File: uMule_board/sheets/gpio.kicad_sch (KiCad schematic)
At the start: 5 parts, among them J10 Conn_02x04_Odd_Even, J11 Conn_01x04, J12 Conn_01x04, J13 Conn_01x04, J9 Conn_02x04_Odd_Even

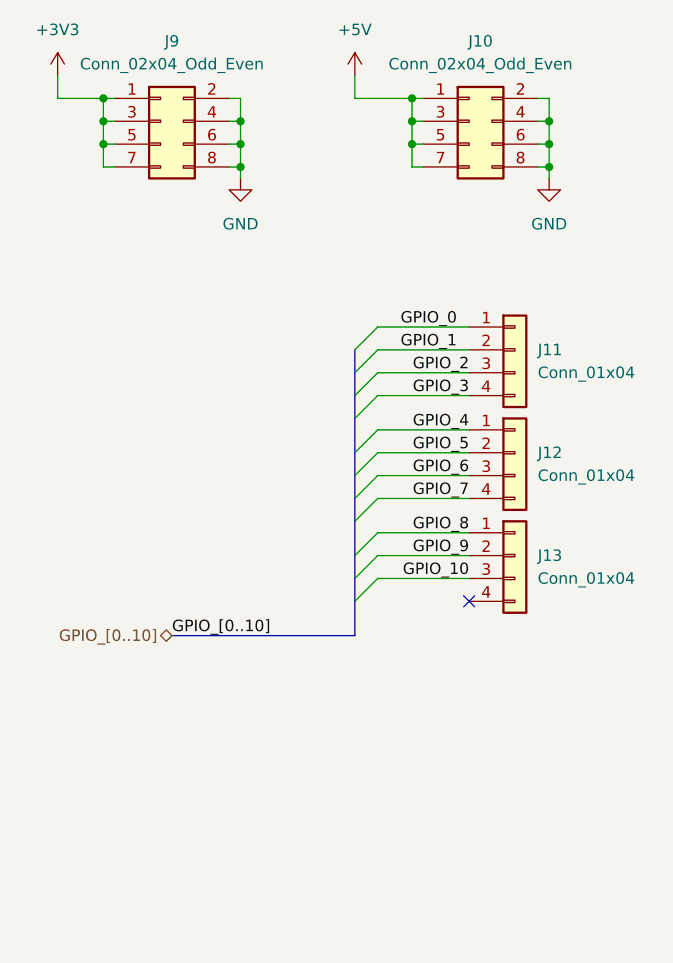
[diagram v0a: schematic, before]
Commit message: Started working on PCB. Ditched high power outputs. Focusing on photodiodes. One commit closer to order
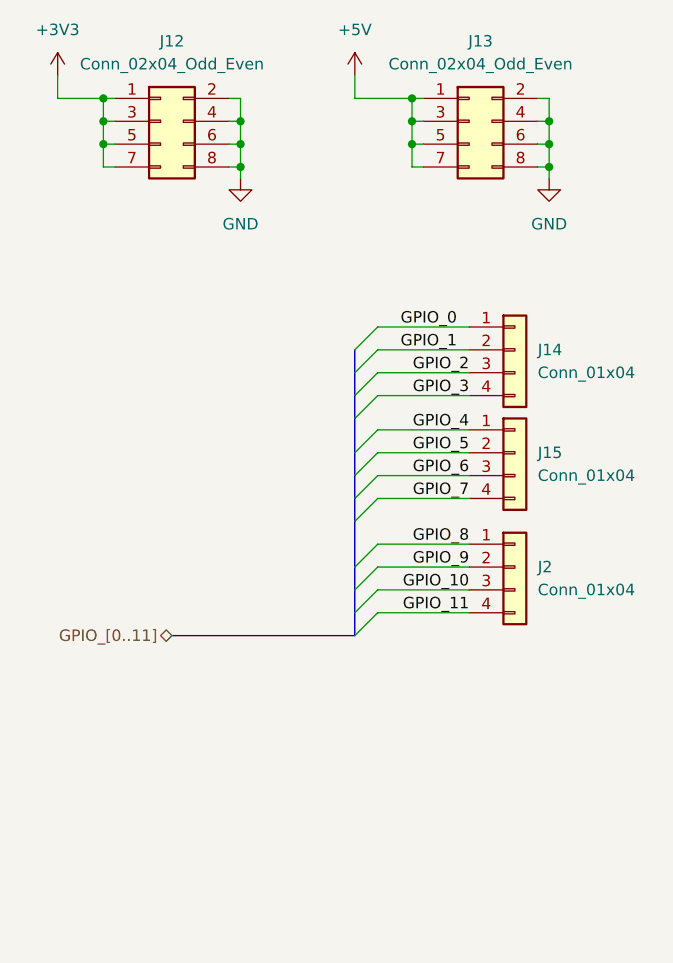
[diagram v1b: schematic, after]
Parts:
- removed J13: Conn_01x04, Connector_PinHeader_2.54mm:PinHeader_1x04_P2.54mm_Vertical, symbol Connector_Generic:Conn_01x04
- added J2: Conn_01x04, Connector_PinHeader_2.54mm:PinHeader_1x04_P2.54mm_Vertical, symbol Connector_Generic:Conn_01x04
- renumbered J9 to J12, J10 to J13, J11 to J14, J12 to J15
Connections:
- net GPIO_10: now also J2.3 (Pin_3)
- net GPIO_8: now also J2.1 (Pin_1)
- net GPIO_9: now also J2.2 (Pin_2)
- new net GPIO_11: J2.4 (Pin_4)
- no-connect marks 1 -> 0
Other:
- title: (none) -> uMule_board

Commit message: removed half phototransistors, etc.
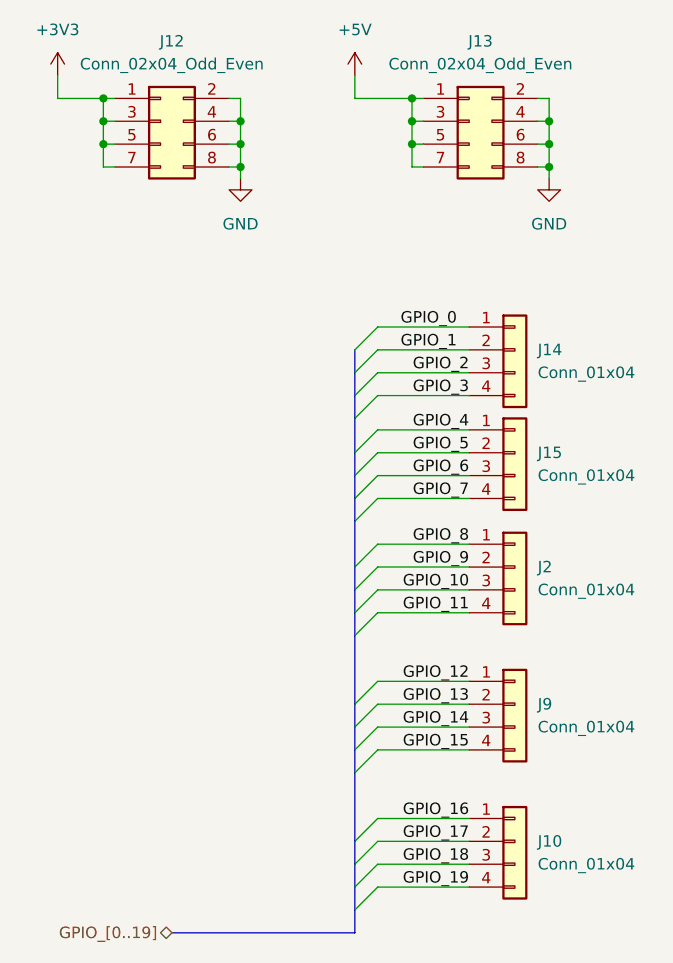
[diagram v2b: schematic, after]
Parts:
- added J10, J9: Conn_01x04, Connector_PinHeader_2.54mm:PinHeader_1x04_P2.54mm_Vertical, symbol Connector_Generic:Conn_01x04
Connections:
- new net GPIO_12: J9.1 (Pin_1)
- new net GPIO_13: J9.2 (Pin_2)
- new net GPIO_14: J9.3 (Pin_3)
- new net GPIO_15: J9.4 (Pin_4)
- new net GPIO_16: J10.1 (Pin_1)
- new net GPIO_17: J10.2 (Pin_2)
- new net GPIO_18: J10.3 (Pin_3)
- new net GPIO_19: J10.4 (Pin_4)

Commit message: sch ready, only missing the pcb
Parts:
- renumbered J14 to J10, J15 to J11, J2 to J12, J9 to J13, J10 to J14, J12 to J8, J13 to J9
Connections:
- net GPIO_0: no longer names the net of J10.1 (Pin_1)
- no-connect marks 0 -> 1
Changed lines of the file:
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@@
 		(color 0 0 0 0)
 	)
+	(no_connect
+		(at 71.12 48.26)
+	)
 	(bus_entry
 		(at 58.42 69.85)
@@
 	)
 	(bus_entry
-		(at 58.42 50.8)
-		(size 2.54 -2.54)
-		(stroke
-			(width 0)
-			(type default)
-		)
-	)
-	(bus_entry
 		(at 58.42 95.25)
 		(size 2.54 -2.54)
@@
 		)
 	)
-	(wire
-		(pts
-			(xy 60.96 48.26) (xy 71.12 48.26)
-		)
-		(stroke
-			(width 0)
-			(type default)
-		)
-	)
 	(bus
 		(pts
@@
 		(pts
 			(xy 60.96 74.93) (xy 71.12 74.93)
-		)
-		(stroke
-			(width 0)
-			(type default)
-		)
-	)
-	(bus
-		(pts
-			(xy 58.42 50.8) (xy 58.42 53.34)
 		)
 		(stroke
@@
 		)
 	)
-	(label "GPIO_0"
-		(at 63.5 48.26 0)
-		(effects
-			(font
-				(size 1.27 1.27)
-			)
-			(justify left bottom)
-		)
-	)
 	(label "GPIO_18"
 		(at 71.12 107.95 180)
@@
 		)
 	)
-	(hierarchical_label "GPIO_[0..19]"
+	(hierarchical_label "GPIO_[1..19]"
 		(shape bidirectional)
 		(at 38.1 115.57 180)
@@
 		(dnp no)
 		(fields_autoplaced yes)
-		(property "Reference" "#PWR0129"
+		(property "Reference" "#PWR093"
 			(at 45.72 38.1 0)
 			(effects
@@
 			(project ""
 				(path "/3d853824-a92e-40a5-ad1a-5052c8a0bd68/88c1cf25-48b5-4442-a726-08f7df56ca6b"
-					(reference "#PWR0129")
+					(reference "#PWR093")
 					(unit 1)
 				)
@@
 		(dnp no)
 		(fields_autoplaced yes)
-		(property "Reference" "J15"
+		(property "Reference" "J11"
 			(at 78.74 62.2299 0)
 			(effects
@@
 			(project "uMule_board"
 				(path "/3d853824-a92e-40a5-ad1a-5052c8a0bd68/88c1cf25-48b5-4442-a726-08f7df56ca6b"
-					(reference "J15")
+					(reference "J11")
 					(unit 1)
 				)
@@
 		(dnp no)
 		(fields_autoplaced yes)
-		(property "Reference" "J13"
+		(property "Reference" "J9"
 			(at 72.39 16.51 0)
 			(effects
@@
 			(project "uMule_board"
 				(path "/3d853824-a92e-40a5-ad1a-5052c8a0bd68/88c1cf25-48b5-4442-a726-08f7df56ca6b"
-					(reference "J13")
+					(reference "J9")
 					(unit 1)
 				)
@@
 		(dnp no)
 		(fields_autoplaced yes)
-		(property "Reference" "#PWR0128"
+		(property "Reference" "#PWR092"
 			(at 58.42 24.13 0)
 			(effects
@@
 			(project ""
 				(path "/3d853824-a92e-40a5-ad1a-5052c8a0bd68/88c1cf25-48b5-4442-a726-08f7df56ca6b"
-					(reference "#PWR0128")
+					(reference "#PWR092")
 					(unit 1)
 				)
@@
 		(dnp no)
 		(fields_autoplaced yes)
-		(property "Reference" "J2"
+		(property "Reference" "J12"
 			(at 78.74 74.9299 0)
 			(effects
@@
 			(project "uMule_board"
 				(path "/3d853824-a92e-40a5-ad1a-5052c8a0bd68/88c1cf25-48b5-4442-a726-08f7df56ca6b"
-					(reference "J2")
+					(reference "J12")
 					(unit 1)
 				)
@@
 		(dnp no)
 		(fields_autoplaced yes)
-		(property "Reference" "J10"
+		(property "Reference" "J14"
 			(at 78.74 105.4099 0)
 			(effects
@@
 			(project "uMule_board"
 				(path "/3d853824-a92e-40a5-ad1a-5052c8a0bd68/88c1cf25-48b5-4442-a726-08f7df56ca6b"
-					(reference "J10")
+					(reference "J14")
 					(unit 1)
 				)
@@
 		(dnp no)
 		(fields_autoplaced yes)
-		(property "Reference" "J9"
+		(property "Reference" "J13"
 			(at 78.74 90.1699 0)
 			(effects
@@
 			(project "uMule_board"
 				(path "/3d853824-a92e-40a5-ad1a-5052c8a0bd68/88c1cf25-48b5-4442-a726-08f7df56ca6b"
-					(reference "J9")
+					(reference "J13")
 					(unit 1)
 				)
@@
 		(dnp no)
 		(fields_autoplaced yes)
-		(property "Reference" "J14"
+		(property "Reference" "J10"
 			(at 78.74 50.7999 0)
 			(effects
@@
 			(project ""
 				(path "/3d853824-a92e-40a5-ad1a-5052c8a0bd68/88c1cf25-48b5-4442-a726-08f7df56ca6b"
-					(reference "J14")
+					(reference "J10")
 					(unit 1)
 				)
@@
 		(dnp no)
 		(fields_autoplaced yes)
-		(property "Reference" "#PWR0130"
+		(property "Reference" "#PWR094"
 			(at 80.01 38.1 0)
 			(effects
@@
 			(project "uMule_board"
 				(path "/3d853824-a92e-40a5-ad1a-5052c8a0bd68/88c1cf25-48b5-4442-a726-08f7df56ca6b"
-					(reference "#PWR0130")
+					(reference "#PWR094")
 					(unit 1)
 				)
@@
 		(dnp no)
 		(fields_autoplaced yes)
-		(property "Reference" "#PWR0127"
+		(property "Reference" "#PWR091"
 			(at 25.4 24.13 0)
 			(effects
@@
 			(project ""
 				(path "/3d853824-a92e-40a5-ad1a-5052c8a0bd68/88c1cf25-48b5-4442-a726-08f7df56ca6b"
-					(reference "#PWR0127")
+					(reference "#PWR091")
 					(unit 1)
 				)
@@
 		(dnp no)
 		(fields_autoplaced yes)
-		(property "Reference" "J12"
+		(property "Reference" "J8"
 			(at 38.1 16.51 0)
 			(effects
@@
 			(project ""
 				(path "/3d853824-a92e-40a5-ad1a-5052c8a0bd68/88c1cf25-48b5-4442-a726-08f7df56ca6b"
-					(reference "J12")
+					(reference "J8")
 					(unit 1)
 				)

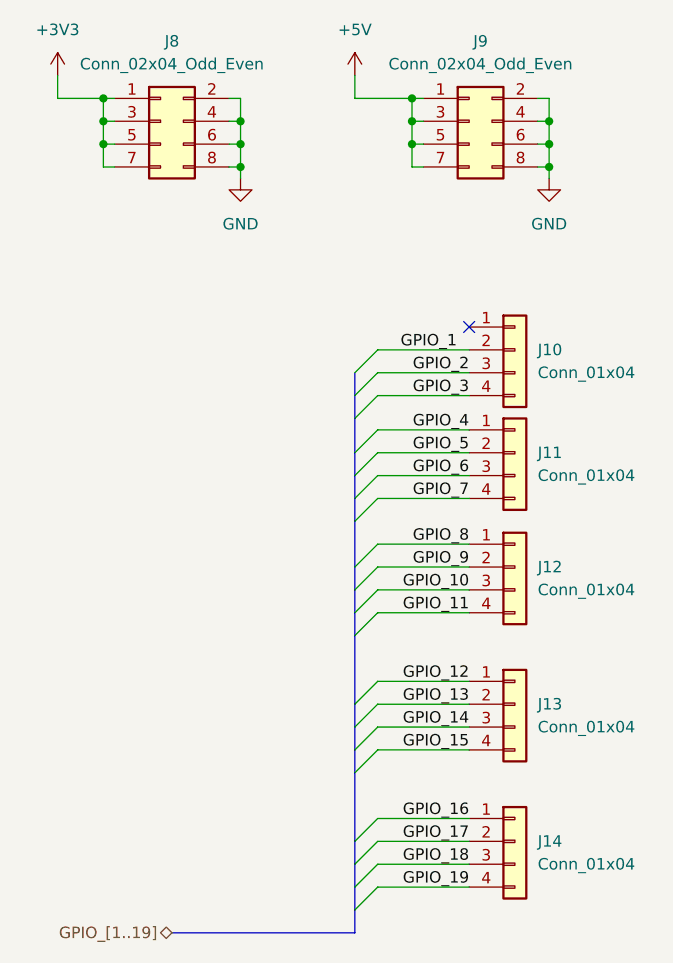
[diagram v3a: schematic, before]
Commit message: DRC Passed, now only slight modifications on traces left, lenght matching and proper board description
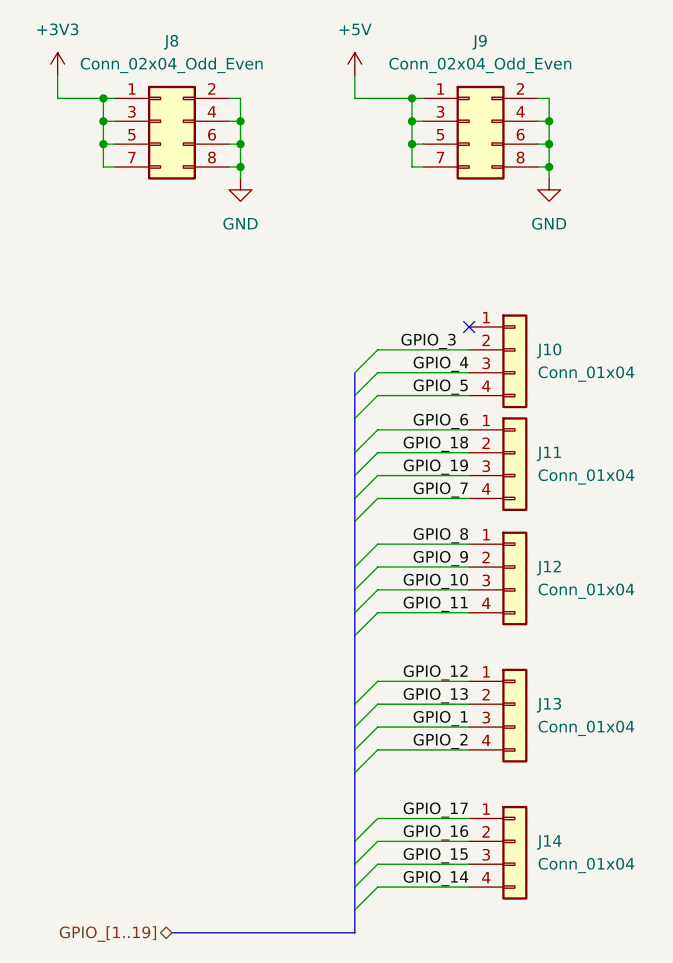
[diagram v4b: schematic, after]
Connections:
- net GPIO_1: now also J13.3 (Pin_3); no longer J10.2 (Pin_2)
- net GPIO_14: now also J14.4 (Pin_4); no longer J13.3 (Pin_3)
- net GPIO_15: now also J14.3 (Pin_3); no longer J13.4 (Pin_4)
- net GPIO_16: now also J14.2 (Pin_2); no longer J14.1 (Pin_1)
- net GPIO_17: now also J14.1 (Pin_1); no longer J14.2 (Pin_2)
- net GPIO_18: now also J11.2 (Pin_2); no longer J14.3 (Pin_3)
- net GPIO_19: now also J11.3 (Pin_3); no longer J14.4 (Pin_4)
- net GPIO_2: now also J13.4 (Pin_4); no longer J10.3 (Pin_3)
- net GPIO_3: now also J10.2 (Pin_2); no longer J10.4 (Pin_4)
- net GPIO_4: now also J10.3 (Pin_3); no longer J11.1 (Pin_1)
- net GPIO_5: now also J10.4 (Pin_4); no longer J11.2 (Pin_2)
- net GPIO_6: now also J11.1 (Pin_1); no longer J11.3 (Pin_3)
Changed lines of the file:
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@@
 		)
 	)
-	(label "GPIO_5"
+	(label "GPIO_18"
 		(at 71.12 62.23 180)
 		(effects
@@
 		)
 	)
-	(label "GPIO_6"
+	(label "GPIO_19"
 		(at 71.12 64.77 180)
 		(effects
@@
 		)
 	)
-	(label "GPIO_17"
+	(label "GPIO_16"
 		(at 71.12 105.41 180)
 		(effects
@@
 		)
 	)
-	(label "GPIO_1"
+	(label "GPIO_3"
 		(at 63.5 50.8 0)
 		(effects
@@
 		)
 	)
-	(label "GPIO_15"
+	(label "GPIO_2"
 		(at 71.12 95.25 180)
 		(effects
@@
 		)
 	)
-	(label "GPIO_3"
+	(label "GPIO_5"
 		(at 71.12 55.88 180)
 		(effects
@@
 		)
 	)
-	(label "GPIO_16"
+	(label "GPIO_17"
 		(at 71.12 102.87 180)
 		(effects
@@
 		)
 	)
-	(label "GPIO_18"
+	(label "GPIO_15"
 		(at 71.12 107.95 180)
 		(effects
@@
 		)
 	)
-	(label "GPIO_14"
+	(label "GPIO_1"
 		(at 71.12 92.71 180)
 		(effects
@@
 		)
 	)
-	(label "GPIO_2"
+	(label "GPIO_4"
 		(at 71.12 53.34 180)
 		(effects
@@
 		)
 	)
-	(label "GPIO_19"
+	(label "GPIO_14"
 		(at 71.12 110.49 180)
 		(effects
@@
 		)
 	)
-	(label "GPIO_4"
+	(label "GPIO_6"
 		(at 71.12 59.69 180)
 		(effects

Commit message: initial board is ready for conecting
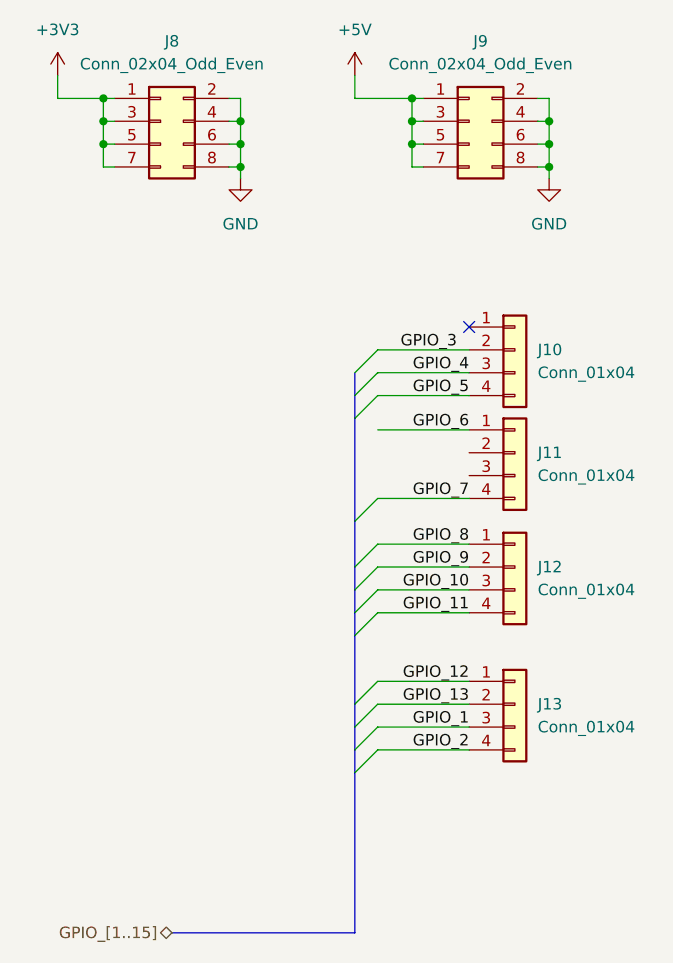
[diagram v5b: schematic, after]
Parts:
- removed J14: Conn_01x04, Connector_PinHeader_2.54mm:PinHeader_1x04_P2.54mm_Vertical, symbol Connector_Generic:Conn_01x04
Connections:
- net GPIO_18: no longer names the net of J11.2 (Pin_2)
- net GPIO_19: no longer names the net of J11.3 (Pin_3)

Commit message: All elements connected. Now making more vias and corrections
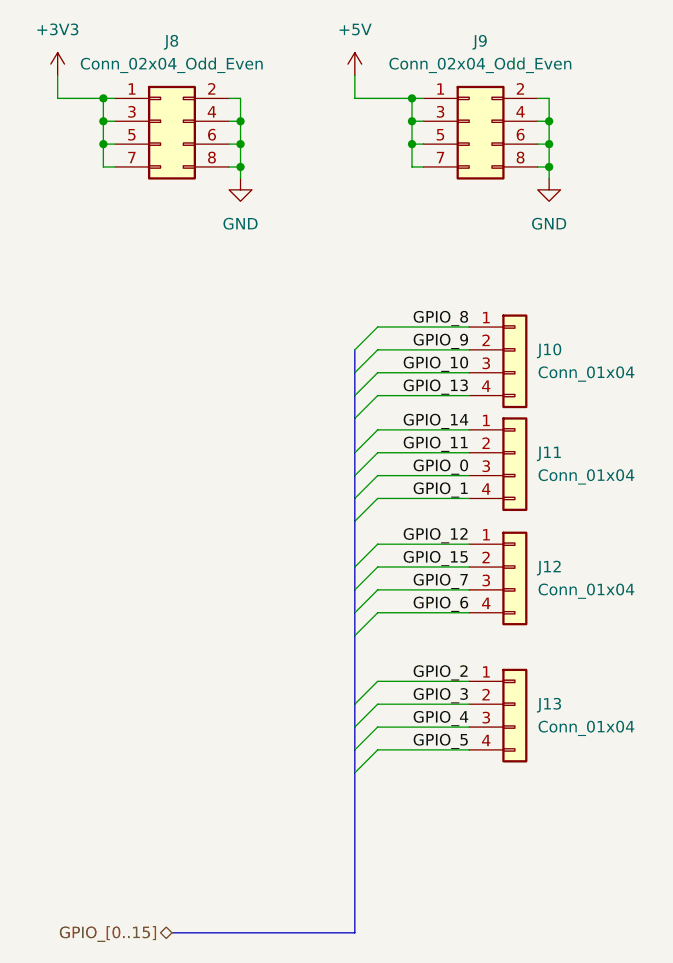
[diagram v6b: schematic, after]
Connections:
- net GPIO_1: now also J11.4 (Pin_4); no longer J13.3 (Pin_3)
- net GPIO_10: now also J10.3 (Pin_3); no longer J12.3 (Pin_3)
- net GPIO_11: now also J11.2 (Pin_2); no longer J12.4 (Pin_4)
- net GPIO_12: now also J12.1 (Pin_1); no longer J13.1 (Pin_1)
- net GPIO_13: now also J10.4 (Pin_4); no longer J13.2 (Pin_2)
- net GPIO_2: now also J13.1 (Pin_1); no longer J13.4 (Pin_4)
- net GPIO_3: now also J13.2 (Pin_2); no longer J10.2 (Pin_2)
- net GPIO_4: now also J13.3 (Pin_3); no longer J10.3 (Pin_3)
- net GPIO_5: now also J13.4 (Pin_4); no longer J10.4 (Pin_4)
- net GPIO_6: now also J12.4 (Pin_4); no longer J11.1 (Pin_1)
- net GPIO_7: now also J12.3 (Pin_3); no longer J11.4 (Pin_4)
- net GPIO_8: now also J10.1 (Pin_1); no longer J12.1 (Pin_1)
- net GPIO_9: now also J10.2 (Pin_2); no longer J12.2 (Pin_2)
- net GPIO_0: now reaches J11.3 (Pin_3)
- new net GPIO_14: J11.1 (Pin_1)
- new net GPIO_15: J12.2 (Pin_2)
- no-connect marks 1 -> 0
